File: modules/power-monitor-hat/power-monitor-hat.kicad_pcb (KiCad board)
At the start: 2 copper layers, 65 x 56 mm, 53 parts, among them J1 Barrel_Jack_Switch, J2 GPIO, J3 OutputTerminal, J4 OutputTerminal, J5 OutputTerminal, Q1 BC856BDW1, Q2 SI2301CDS, U1 CAT24C256, U2 NCP1117-3.3_SOT223, U3 INA219AxD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

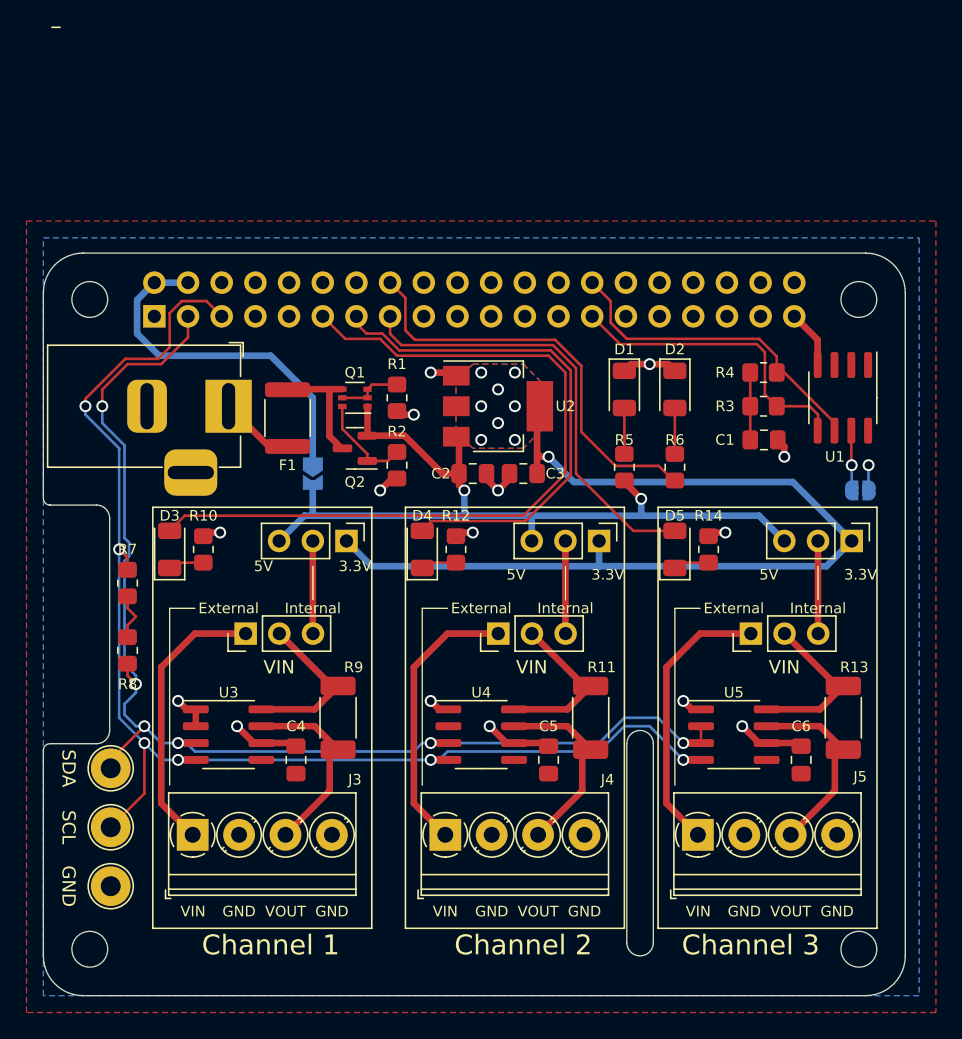
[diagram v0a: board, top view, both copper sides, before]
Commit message: Add separate net for "power ground"
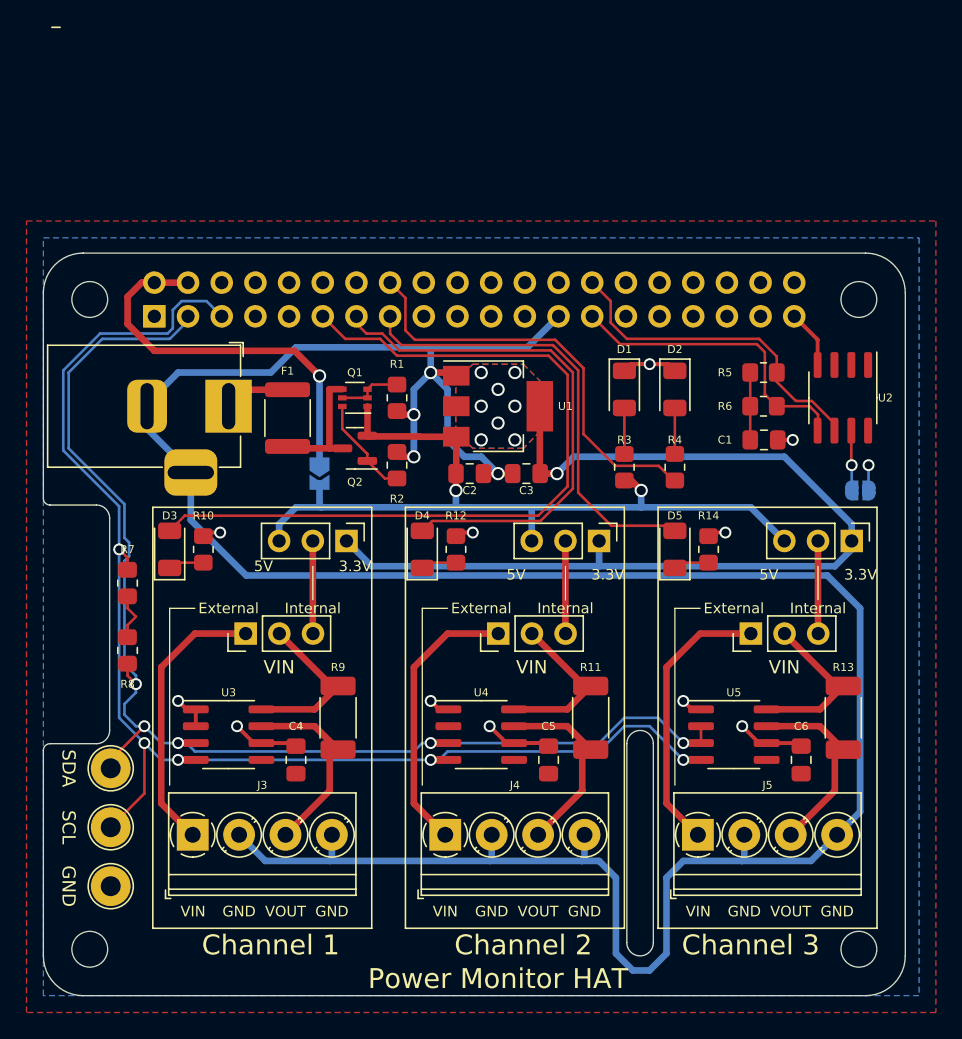
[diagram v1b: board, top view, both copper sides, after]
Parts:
- C4, C5, C6: value C -> 100n
- moved JP1 0.51 mm to (120.8, 60.6)
- moved C3 0.23 mm to (136.4, 60.6)
- moved C2 0.23 mm to (132.2, 60.6)
- turned F1 to -90 degrees
- turned R2 to 90 degrees
- renumbered R5 to R3, R6 to R4, R4 to R5, R3 to R6, U2 to U1, U1 to U2
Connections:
- C2 pad 2: GND -> GNDPWR
- C3 pad 2: GND -> GNDPWR
- J1 pad 2: GND -> GNDPWR
- J1 pad 3: GND -> GNDPWR
- J2 pad 25: GND -> GNDPWR
- J3 pad 2: GND -> GNDPWR
- J3 pad 4: GND -> GNDPWR
- J4 pad 2: GND -> GNDPWR
- J4 pad 4: GND -> GNDPWR
- J5 pad 2: GND -> GNDPWR
- J5 pad 4: GND -> GNDPWR
- R1 pad 2: GND -> GNDPWR
- R2 pad 2: GND -> GNDPWR
- U1 pad 1: GND -> GNDPWR
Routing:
- net GNDPWR: track 0.00 -> 209.6 mm, vias 0 -> 4
- net GND: track 40.8 -> 34.0 mm, vias 15 -> 11
- net /SDA: track 90.4 -> 94.0 mm, vias 6 -> 5
- net /SCL: track 98.3 -> 101.2 mm, vias 6 -> 5
- net +5V: track 27.2 -> 29.8 mm, vias 0 -> 1
- net +3.3VP: track 72.9 -> 74.4 mm
- net /ID_SCL: track 24.3 -> 25.3 mm
- net +5VP: track 63.3 -> 62.5 mm
- net /LED_CH2: track 38.5 -> 39.3 mm
- net /LED_CH1: track 59.3 -> 60.1 mm
- net /LED_CH3: track 33.6 -> 34.3 mm
- net /Vfused: track 8.96 -> 9.64 mm
- net /Vpsu: track 4.32 -> 4.96 mm
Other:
- board text added: "Power Monitor HAT"

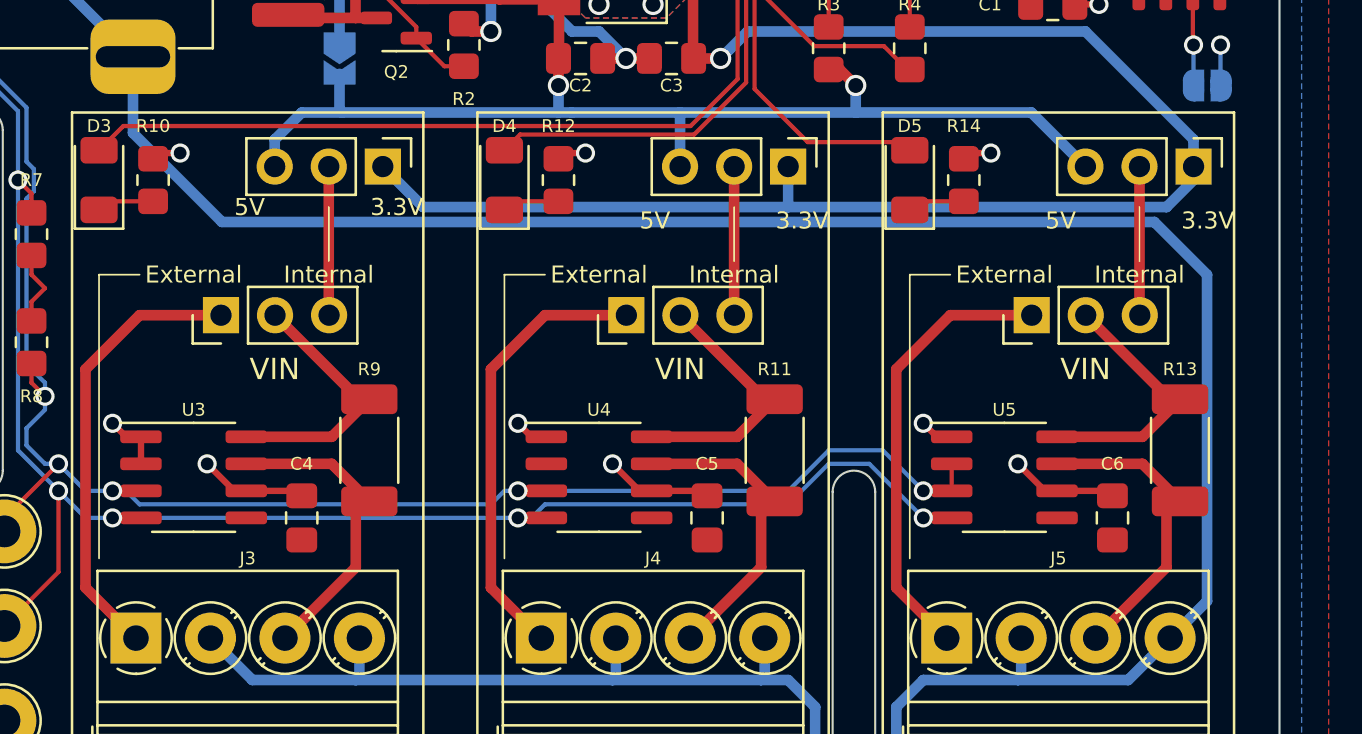
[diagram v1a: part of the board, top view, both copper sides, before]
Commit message: Change footprint for jumpers to "no first pin" version
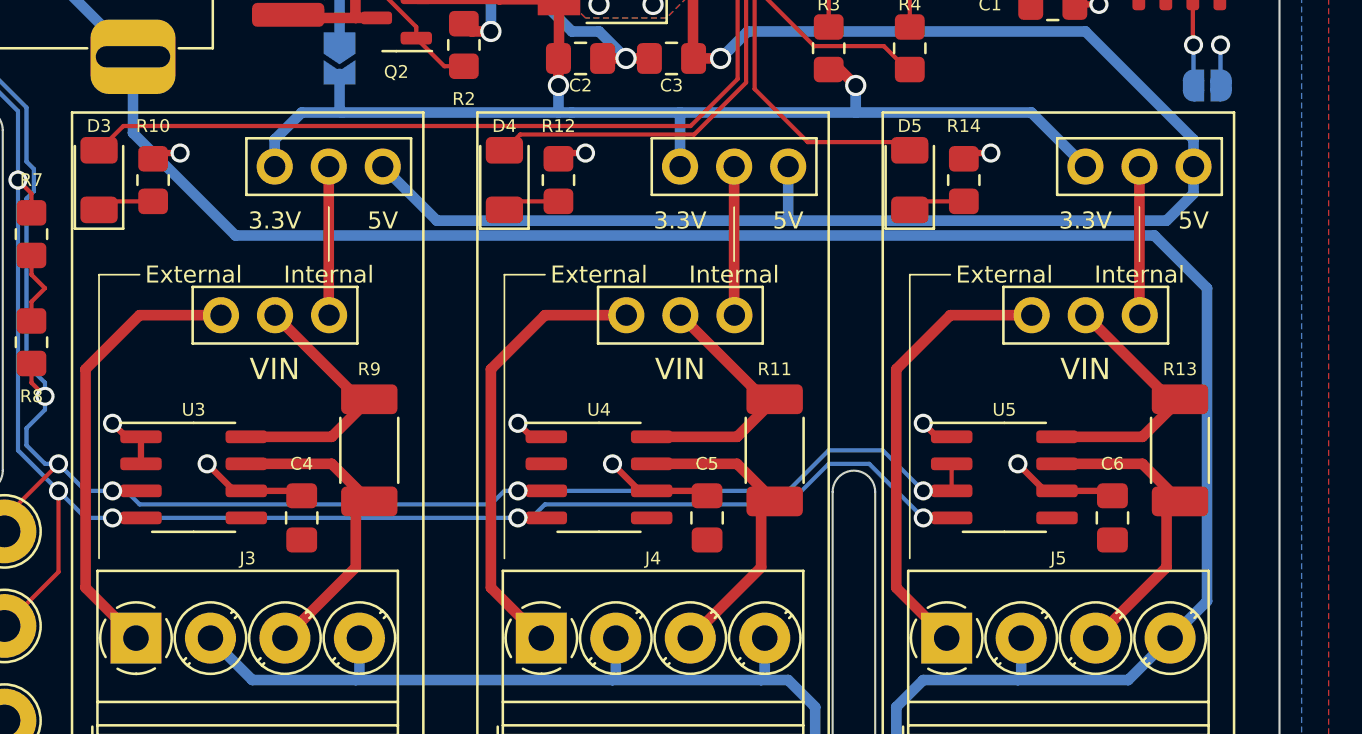
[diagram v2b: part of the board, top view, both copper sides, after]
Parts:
- JP3, JP4, JP5, JP6, JP7, JP8: footprint Connector_PinHeader_2.54mm:PinHeader_1x03_P2.54mm_Vertical -> shared_components:PinHeader_1x03_P2.54mm_Vertical_NoFP
- moved JP8 5.08 mm to (155.9, 65.7), turned to 90 degrees
- moved JP4 5.08 mm to (117.8, 65.7), turned to 90 degrees
- moved JP6 5.08 mm to (136.8, 65.7), turned to 90 degrees
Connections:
- JP4 pad 1: +3.3VP -> +5VP
- JP4 pad 3: +5VP -> +3.3VP
- JP6 pad 1: +3.3VP -> +5VP
- JP6 pad 3: +5VP -> +3.3VP
- JP8 pad 1: +3.3VP -> +5VP
- JP8 pad 3: +5VP -> +3.3VP
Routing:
- net +3.3VP: track 74.4 -> 76.0 mm

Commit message: Enhancements
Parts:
- R11, R13, R9: value R -> 0R5
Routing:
- net /SCL: track 101.2 -> 103.6 mm
- net /SDA: track 94.0 -> 96.1 mm

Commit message: Improve silkscreen, add version and symbols
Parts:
- added SYM1: Symbol_Barrel_Polarity, Symbol:Symbol_Barrel_Polarity, F.Cu at (104.4, 61.3)
- added SYM2: OSHW-Logo2_7.3x6mm_SilkScreen, Symbol:OSHW-Logo2_7.3x6mm_SilkScreen, B.Cu at (125.4, 96.2)
- added SYM3: KiCad-Logo2_5mm_SilkScreen, Symbol:KiCad-Logo2_5mm_SilkScreen, B.Cu at (112.7, 96.2)
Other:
- board text added: "v1.0"

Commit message: Improve silkscreen cd
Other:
- board text added: "5V"
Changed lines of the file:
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@@
     (property "Sheetname" "")
     (attr smd)
-    (fp_text reference "R1" (at -2.54 0) (layer "F.SilkS")
-      (effects (font (size 0.6 0.6) (thickness 0.08)))
+    (fp_text reference "R1" (at 0 -1.27) (layer "F.SilkS")
+      (effects (font (size 0.6 0.6) (thickness 0.08)) (justify left))
     )
-    (fp_text value "10k" (at 0 -1.905 -180) (layer "F.Fab")
+    (fp_text value "10k" (at 1.905 0 -180) (layer "F.Fab")
       (effects (font (size 0.6 0.6) (thickness 0.08)))
     )
@@
     (property "Sheetname" "")
     (attr smd)
-    (fp_text reference "R2" (at -2.54 0) (layer "F.SilkS")
-      (effects (font (size 0.6 0.6) (thickness 0.08)))
+    (fp_text reference "R2" (at 0 1.27) (layer "F.SilkS")
+      (effects (font (size 0.6 0.6) (thickness 0.08)) (justify left))
     )
-    (fp_text value "47k" (at 0 1.905 180) (layer "F.Fab")
+    (fp_text value "47k" (at -1.905 0 180) (layer "F.Fab")
       (effects (font (size 0.6 0.6) (thickness 0.08)))
     )
@@
     (property "Sheetname" "")
     (attr smd)
-    (fp_text reference "U2" (at 0 -3.8425 180) (layer "F.SilkS")
+    (fp_text reference "U2" (at 4.445 0.6025 180) (layer "F.SilkS")
       (effects (font (size 0.6 0.6) (thickness 0.08)))
     )
@@
     (effects (font (size 0.8 0.8) (thickness 0.15)))
   )
-  (gr_text "Power Monitor HAT" (at 134.29 98.73) (layer "F.SilkS")
+  (gr_text "Power Monitor HAT" (at 132.385 98.73) (layer "F.SilkS")
     (effects (font (size 1.5 1.5) (thickness 0.3)))
   )
@@
     (effects (font (size 0.8 0.8) (thickness 0.15)))
   )
-  (gr_text "v1.0" (at 146.99 98.73) (layer "F.SilkS")
+  (gr_text "v1.0" (at 145.085 98.73) (layer "F.SilkS")
     (effects (font (size 0.8 0.8) (thickness 0.1)))
   )
@@
     (effects (font (size 0.8 0.8) (thickness 0.15)))
   )
+  (gr_text "5V" (at 114.605 61.265) (layer "F.SilkS")
+    (effects (font (size 1 1) (thickness 0.15)))
+  )
   (gr_text "USB" (at 177.724 71.552) (layer "Dwgs.User")

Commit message: Tract improvements
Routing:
- net +3.3V: track 10.6 -> 6.96 mm
- net /PowerChannel 2/VIN: track 11.9 -> 13.2 mm
- net /PowerChannel 3/VIN: track 11.9 -> 13.2 mm
- net /PowerChannel 2/VOUT: track 14.3 -> 15.2 mm
- net /PowerChannel 1/VOUT: track 14.3 -> 15.2 mm
- net /PowerChannel 3/VOUT: track 14.3 -> 15.2 mm
- net /PowerChannel 1/VIN: track 12.6 -> 13.2 mm
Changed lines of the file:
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@@
     (grid_origin 100 100)
     (pcbplotparams
-      (layerselection 0x0000030_80000001)
+      (layerselection 0x00000f0_ffffffff)
       (disableapertmacros false)
       (usegerberextensions true)
@@
       (outputformat 1)
       (mirror false)
-      (drillshape 1)
+      (drillshape 0)
       (scaleselection 1)
-      (outputdirectory "")
+      (outputdirectory "gerbers")
     )
   )
@@
   (via (at 120.828 53.264) (size 1) (drill 0.7) (layers "F.Cu" "B.Cu") (net 25))
   (segment (start 120.828 53.264) (end 120.828 59.868) (width 0.5) (layer "B.Cu") (net 25))
-  (segment (start 106.35 72.06) (end 106.985 71.425) (width 0.2) (layer "F.Cu") (net 26))
   (segment (start 153.3075 55.55) (end 153.3075 58.09) (width 0.2) (layer "F.Cu") (net 26))
   (segment (start 153.3075 53.01) (end 153.3075 55.55) (width 0.2) (layer "F.Cu") (net 26))
-  (segment (start 106.35 72.965) (end 106.35 72.06) (width 0.2) (layer "F.Cu") (net 26))
-  (segment (start 106.35 69.885) (end 106.35 70.79) (width 0.2) (layer "F.Cu") (net 26))
-  (segment (start 106.35 70.79) (end 106.985 71.425) (width 0.2) (layer "F.Cu") (net 26))
   (via (at 162.23 59.995) (size 0.9) (drill 0.6) (layers "F.Cu" "B.Cu") (free) (net 26))
   (segment (start 162.23 59.995) (end 162.23 61.87) (width 0.2) (layer "B.Cu") (net 26))
@@
   (segment (start 108.89 75.235) (end 108.89 85.5) (width 0.5) (layer "F.Cu") (net 27))
   (segment (start 111.43 72.695) (end 108.89 75.235) (width 0.5) (layer "F.Cu") (net 27))
-  (segment (start 116.445 79.68) (end 120.46 79.68) (width 0.5) (layer "F.Cu") (net 28))
-  (segment (start 121.59 84.54) (end 118.26 87.87) (width 0.5) (layer "F.Cu") (net 28))
-  (segment (start 120.46 79.68) (end 122.225 81.445) (width 0.5) (layer "F.Cu") (net 28))
-  (segment (start 121.59 81.445) (end 121.59 84.54) (width 0.5) (layer "F.Cu") (net 28))
+  (segment (start 121.59 79.68) (end 122.225 80.315) (width 0.5) (layer "F.Cu") (net 28))
+  (segment (start 122.225 80.315) (end 122.225 81.445) (width 0.5) (layer "F.Cu") (net 28))
+  (segment (start 122.225 83.905) (end 118.26 87.87) (width 0.5) (layer "F.Cu") (net 28))
+  (segment (start 116.445 79.68) (end 121.59 79.68) (width 0.5) (layer "F.Cu") (net 28))
+  (segment (start 122.225 81.445) (end 122.225 83.905) (width 0.5) (layer "F.Cu") (net 28))
   (segment (start 130.48 72.695) (end 127.94 75.235) (width 0.5) (layer "F.Cu") (net 29))
   (segment (start 134.305 72.695) (end 130.48 72.695) (width 0.5) (layer "F.Cu") (net 29))
   (segment (start 127.94 75.235) (end 127.94 85.5) (width 0.5) (layer "F.Cu") (net 29))
   (segment (start 127.94 85.5) (end 130.31 87.87) (width 0.5) (layer "F.Cu") (net 29))
-  (segment (start 140.64 84.54) (end 137.31 87.87) (width 0.5) (layer "F.Cu") (net 30))
-  (segment (start 140.64 81.445) (end 140.64 84.54) (width 0.5) (layer "F.Cu") (net 30))
-  (segment (start 139.51 79.68) (end 141.275 81.445) (width 0.5) (layer "F.Cu") (net 30))
-  (segment (start 135.495 79.68) (end 139.51 79.68) (width 0.5) (layer "F.Cu") (net 30))
+  (segment (start 135.495 79.68) (end 140.64 79.68) (width 0.5) (layer "F.Cu") (net 30))
+  (segment (start 141.275 81.445) (end 141.275 83.905) (width 0.5) (layer "F.Cu") (net 30))
+  (segment (start 141.275 83.905) (end 137.31 87.87) (width 0.5) (layer "F.Cu") (net 30))
+  (segment (start 141.275 80.315) (end 141.275 81.445) (width 0.5) (layer "F.Cu") (net 30))
+  (segment (start 140.64 79.68) (end 141.275 80.315) (width 0.5) (layer "F.Cu") (net 30))
   (segment (start 149.53 72.695) (end 146.99 75.235) (width 0.5) (layer "F.Cu") (net 31))
   (segment (start 146.99 85.5) (end 149.36 87.87) (width 0.5) (layer "F.Cu") (net 31))
   (segment (start 146.99 75.235) (end 146.99 85.5) (width 0.5) (layer "F.Cu") (net 31))
   (segment (start 153.355 72.695) (end 149.53 72.695) (width 0.5) (layer "F.Cu") (net 31))
-  (segment (start 158.56 79.68) (end 160.325 81.445) (width 0.5) (layer "F.Cu") (net 32))
-  (segment (start 154.545 79.68) (end 158.56 79.68) (width 0.5) (layer "F.Cu") (net 32))
-  (segment (start 159.69 81.445) (end 159.69 84.54) (width 0.5) (layer "F.Cu") (net 32))
-  (segment (start 159.69 84.54) (end 156.36 87.87) (width 0.5) (layer "F.Cu") (net 32))
+  (segment (start 159.69 79.68) (end 160.325 80.315) (width 0.5) (layer "F.Cu") (net 32))
+  (segment (start 160.325 81.445) (end 160.325 83.905) (width 0.5) (layer "F.Cu") (net 32))
+  (segment (start 154.545 79.68) (end 159.69 79.68) (width 0.5) (layer "F.Cu") (net 32))
+  (segment (start 160.325 83.905) (end 156.36 87.87) (width 0.5) (layer "F.Cu") (net 32))
+  (segment (start 160.325 80.315) (end 160.325 81.445) (width 0.5) (layer "F.Cu") (net 32))
   (segment (start 160.9275 57.39) (end 160.9275 59.9625) (width 0.2) (layer "F.Cu") (net 33))
   (segment (start 160.9275 59.9625) (end 160.96 59.995) (width 0.2) (layer "F.Cu") (net 33))
   (via (at 160.96 59.995) (size 0.9) (drill 0.6) (layers "F.Cu" "B.Cu") (net 33))
   (segment (start 160.96 59.995) (end 160.96 61.9) (width 0.2) (layer "B.Cu") (net 33))
-  (segment (start 120.46 78.41) (end 122.225 76.645) (width 0.5) (layer "F.Cu") (net 34))
-  (segment (start 117.795 72.695) (end 121.745 76.645) (width 0.5) (layer "F.Cu") (net 34))
+  (segment (start 121.59 78.41) (end 116.445 78.41) (width 0.5) (layer "F.Cu") (net 34))
   (segment (start 121.745 76.645) (end 122.225 76.645) (width 0.5) (layer "F.Cu") (net 34))
-  (segment (start 116.445 78.41) (end 120.46 78.41) (width 0.5) (layer "F.Cu") (net 34))
+  (segment (start 122.225 77.775) (end 121.59 78.41) (width 0.5) (layer "F.Cu") (net 34))
+  (segment (start 122.225 76.645) (end 122.225 77.775) (width 0.5) (layer "F.Cu") (net 34))
+  (segment (start 117.795 72.695) (end 121.745 76.645) (width 0.5) (layer "F.Cu") (net 34))
   (segment (start 120.32 65.71) (end 120.32 72.68) (width 0.5) (layer "F.Cu") (net 35))
-  (segment (start 139.51 78.41) (end 141.275 76.645) (width 0.5) (layer "F.Cu") (net 36))
-  (segment (start 135.495 78.41) (end 139.51 78.41) (width 0.5) (layer "F.Cu") (net 36))
-  (segment (start 136.845 72.695) (end 140.64 76.49) (width 0.5) (layer "F.Cu") (net 36))
+  (segment (start 140.64 78.41) (end 141.275 77.775) (width 0.5) (layer "F.Cu") (net 36))
+  (segment (start 141.275 76.645) (end 140.795 76.645) (width 0.5) (layer "F.Cu") (net 36))
+  (segment (start 141.275 77.775) (end 141.275 76.645) (width 0.5) (layer "F.Cu") (net 36))
+  (segment (start 140.795 76.645) (end 136.845 72.695) (width 0.5) (layer "F.Cu") (net 36))
+  (segment (start 135.495 78.41) (end 140.64 78.41) (width 0.5) (layer "F.Cu") (net 36))
   (segment (start 139.37 65.71) (end 139.37 72.68) (width 0.5) (layer "F.Cu") (net 37))
-  (segment (start 158.56 78.41) (end 160.325 76.645) (width 0.5) (layer "F.Cu") (net 38))
-  (segment (start 154.545 78.41) (end 158.56 78.41) (width 0.5) (layer "F.Cu") (net 38))
-  (segment (start 155.895 72.695) (end 159.69 76.49) (width 0.5) (layer "F.Cu") (net 38))
+  (segment (start 159.845 76.645) (end 155.895 72.695) (width 0.5) (layer "F.Cu") (net 38))
+  (segment (start 160.325 77.775) (end 160.325 76.645) (width 0.5) (layer "F.Cu") (net 38))
+  (segment (start 159.69 78.41) (end 160.325 77.775) (width 0.5) (layer "F.Cu") (net 38))
+  (segment (start 160.325 76.645) (end 159.845 76.645) (width 0.5) (layer "F.Cu") (net 38))
+  (segment (start 154.545 78.41) (end 159.69 78.41) (width 0.5) (layer "F.Cu") (net 38))
   (segment (start 158.42 65.71) (end 158.42 72.68) (width 0.5) (layer "F.Cu") (net 39))
   (segment (start 107.62 79.68) (end 105.08 82.22) (width 0.2) (layer "F.Cu") (net 43))
